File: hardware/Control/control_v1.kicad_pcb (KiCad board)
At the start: 2 copper layers, 109.2 x 88.9 mm, 45 parts, among them J1 Conn_02x07_Counter_Clockwise, J2 Screw_Terminal_01x05, J4 RJ45, M1 STM32F4-DISCOVERY, Q1 BCX56, U1 TL2575HV-ADJ, U2 TL2575HV-ADJ, U3 DS89C21

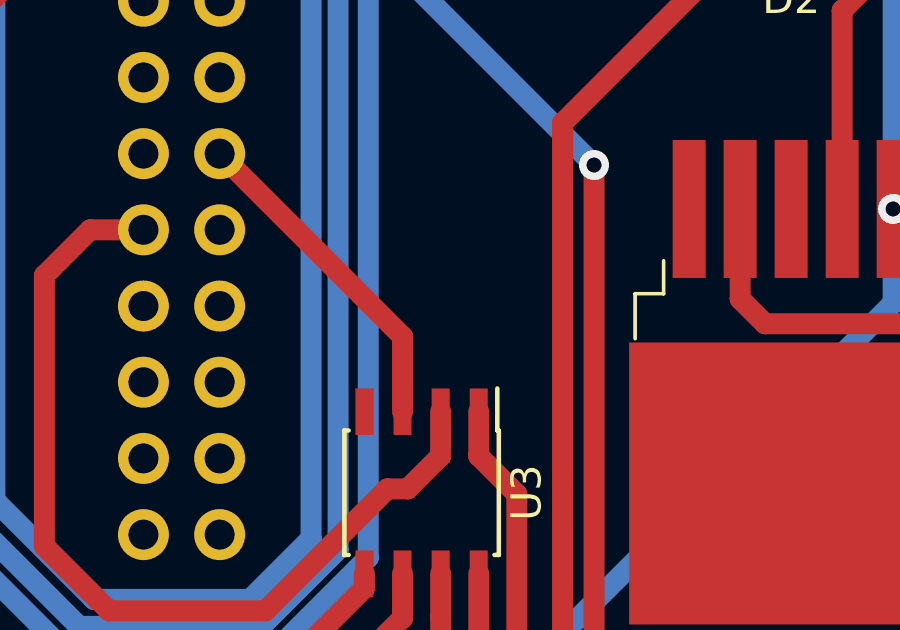
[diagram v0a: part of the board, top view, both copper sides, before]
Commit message: Added decoupling cap for RS485
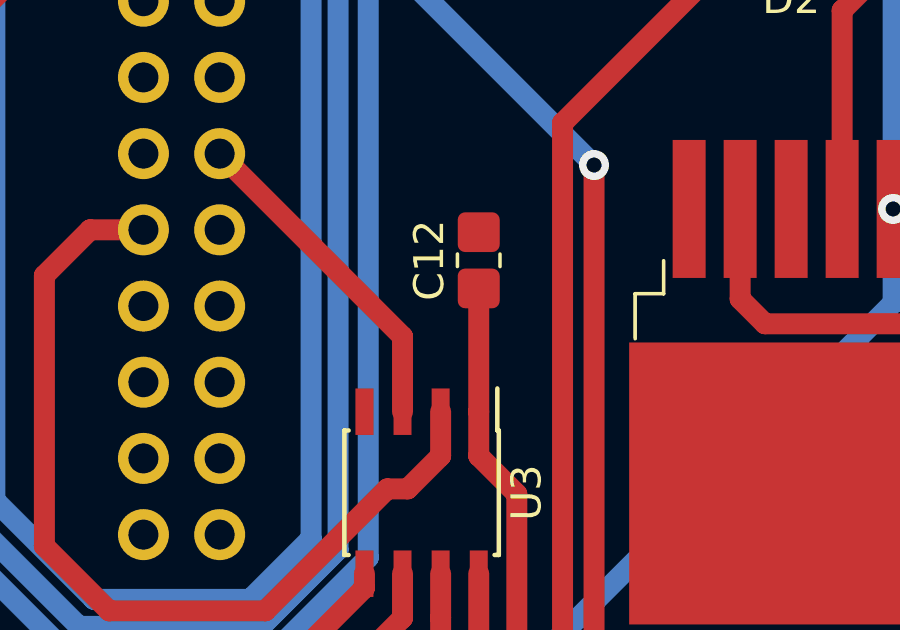
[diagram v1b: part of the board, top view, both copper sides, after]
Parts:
- added C12: 2.2uF, Capacitor_SMD:C_0805_2012Metric_Pad1.33x1.40mm_HandSolder, F.Cu at (143.3, 114.0)
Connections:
- J4 pad 4: (no net) -> Net-(J4-Pad4)
- M1 pad 10: (no net) -> Net-(M1-Pad10)
- M1 pad 12: (no net) -> Net-(M1-Pad12)
- M1 pad 13: (no net) -> Net-(M1-Pad13)
- M1 pad 14: (no net) -> Net-(M1-Pad14)
- M1 pad 15: (no net) -> Net-(M1-Pad15)
- M1 pad 16: (no net) -> Net-(M1-Pad16)
- M1 pad 17: (no net) -> Net-(M1-Pad17)
- M1 pad 18: (no net) -> Net-(M1-Pad18)
- M1 pad 21: (no net) -> Net-(M1-Pad21)
- M1 pad 24: (no net) -> Net-(M1-Pad24)
- M1 pad 25: (no net) -> Net-(M1-Pad25)
- M1 pad 3: (no net) -> Net-(M1-Pad3)
- M1 pad 32: (no net) -> Net-(M1-Pad32)
- M1 pad 33: (no net) -> Net-(M1-Pad33)
- M1 pad 34: (no net) -> Net-(M1-Pad34)
- M1 pad 35: (no net) -> Net-(M1-Pad35)
- M1 pad 36: (no net) -> Net-(M1-Pad36)
- M1 pad 37: (no net) -> Net-(M1-Pad37)
- M1 pad 38: (no net) -> Net-(M1-Pad38)
- M1 pad 39: (no net) -> Net-(M1-Pad39)
- M1 pad 4: (no net) -> Net-(M1-Pad4)
- M1 pad 42: (no net) -> Net-(M1-Pad42)
- M1 pad 43: (no net) -> Net-(M1-Pad43)
- M1 pad 44: (no net) -> Net-(M1-Pad44)
- M1 pad 45: (no net) -> Net-(M1-Pad45)
- M1 pad 46: (no net) -> Net-(M1-Pad46)
- M1 pad 47: (no net) -> Net-(M1-Pad47)
- M1 pad 48: (no net) -> Net-(M1-Pad48)
- M1 pad 55: (no net) -> Net-(M1-Pad55)
- M1 pad 56: (no net) -> Net-(M1-Pad56)
- M1 pad 57: (no net) -> Net-(M1-Pad57)
- M1 pad 58: (no net) -> Net-(M1-Pad58)
- M1 pad 59: (no net) -> Net-(M1-Pad59)
- M1 pad 6: (no net) -> Net-(M1-Pad6)
- M1 pad 60: (no net) -> Net-(M1-Pad60)
- M1 pad 61: (no net) -> Net-(M1-Pad61)
- M1 pad 62: (no net) -> Net-(M1-Pad62)
- M1 pad 63: (no net) -> Net-(M1-Pad63)
- M1 pad 64: (no net) -> Net-(M1-Pad64)
- M1 pad 65: (no net) -> Net-(M1-Pad65)
- M1 pad 66: (no net) -> Net-(M1-Pad66)
- M1 pad 67: (no net) -> Net-(M1-Pad67)
- M1 pad 68: (no net) -> Net-(M1-Pad68)
- M1 pad 69: (no net) -> Net-(M1-Pad69)
- M1 pad 7: (no net) -> Net-(M1-Pad7)
- M1 pad 70: (no net) -> Net-(M1-Pad70)
- M1 pad 71: (no net) -> Net-(M1-Pad71)
- M1 pad 72: (no net) -> Net-(M1-Pad72)
- M1 pad 73: (no net) -> Net-(M1-Pad73)
- M1 pad 74: (no net) -> Net-(M1-Pad74)
- M1 pad 77: (no net) -> Net-(M1-Pad77)
- M1 pad 78: (no net) -> Net-(M1-Pad78)
- M1 pad 79: (no net) -> Net-(M1-Pad79)
- M1 pad 8: (no net) -> Net-(M1-Pad8)
- M1 pad 80: (no net) -> Net-(M1-Pad80)
- M1 pad 81: (no net) -> Net-(M1-Pad81)
- M1 pad 82: (no net) -> Net-(M1-Pad82)
- M1 pad 83: (no net) -> Net-(M1-Pad83)
- M1 pad 84: (no net) -> Net-(M1-Pad84)
- M1 pad 85: (no net) -> Net-(M1-Pad85)
- M1 pad 86: (no net) -> Net-(M1-Pad86)
- M1 pad 87: (no net) -> Net-(M1-Pad87)
- M1 pad 88: (no net) -> Net-(M1-Pad88)
- M1 pad 89: (no net) -> Net-(M1-Pad89)
- M1 pad 90: (no net) -> Net-(M1-Pad90)
- M1 pad 91: (no net) -> Net-(M1-Pad91)
- M1 pad 92: (no net) -> Net-(M1-Pad92)
- M1 pad 93: (no net) -> Net-(M1-Pad93)
- M1 pad 94: (no net) -> Net-(M1-Pad94)
- M1 pad 95: (no net) -> Net-(M1-Pad95)
- M1 pad 96: (no net) -> Net-(M1-Pad96)
- M1 pad 97: (no net) -> Net-(M1-Pad97)
- M1 pad 98: (no net) -> Net-(M1-Pad98)
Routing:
- net /5v: track 259.1 -> 263.2 mm
